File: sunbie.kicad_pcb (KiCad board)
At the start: 2 copper layers, 98 x 98 mm, 22 parts, among them J1 Display, Q1 BC547, SW1 SW_Push_45deg, SW2 SW_Push_45deg, SW3 SW_Push_45deg, SW4 SW_Push_45deg, SW5 SW_Push_45deg, U1 XIAO-ESP32-C3-SMD, U2 LSM6DS3, U3 BME280, U4 TSL25911FN

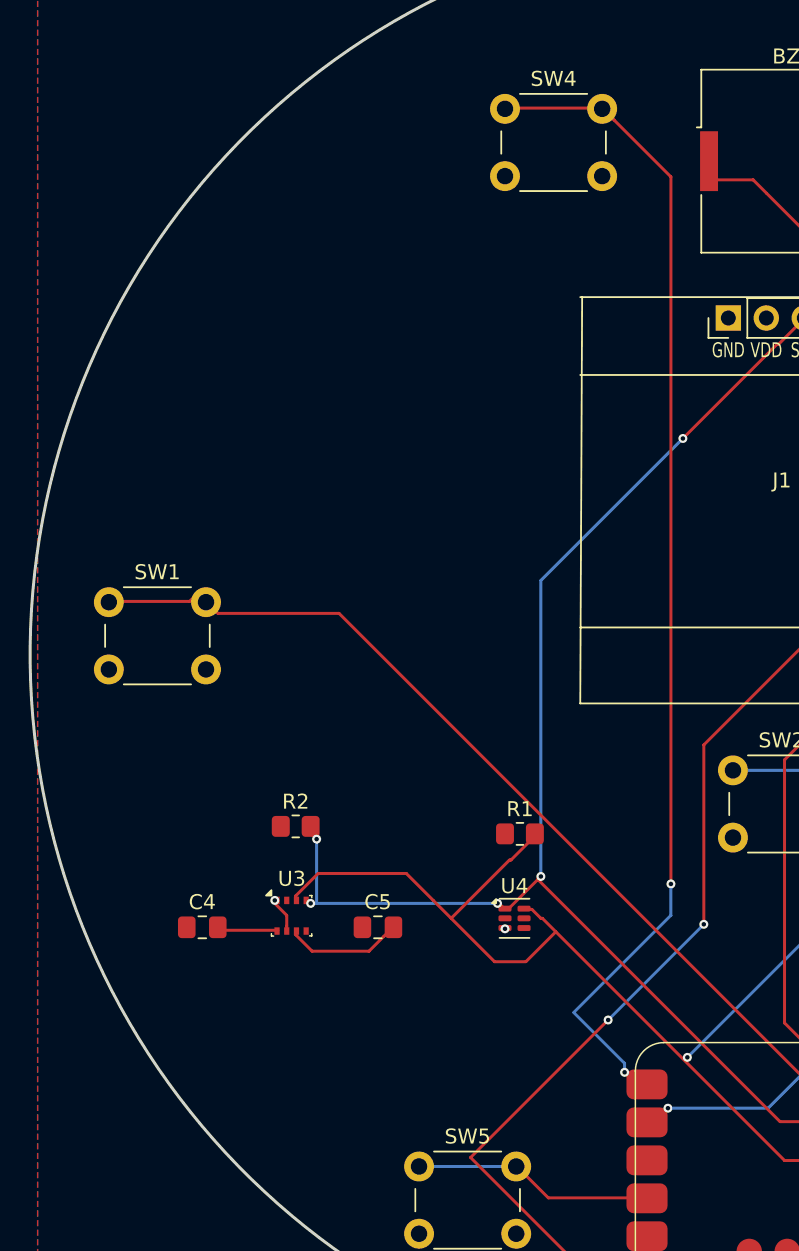
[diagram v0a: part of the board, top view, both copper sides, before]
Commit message: added 2 ws2812 leds
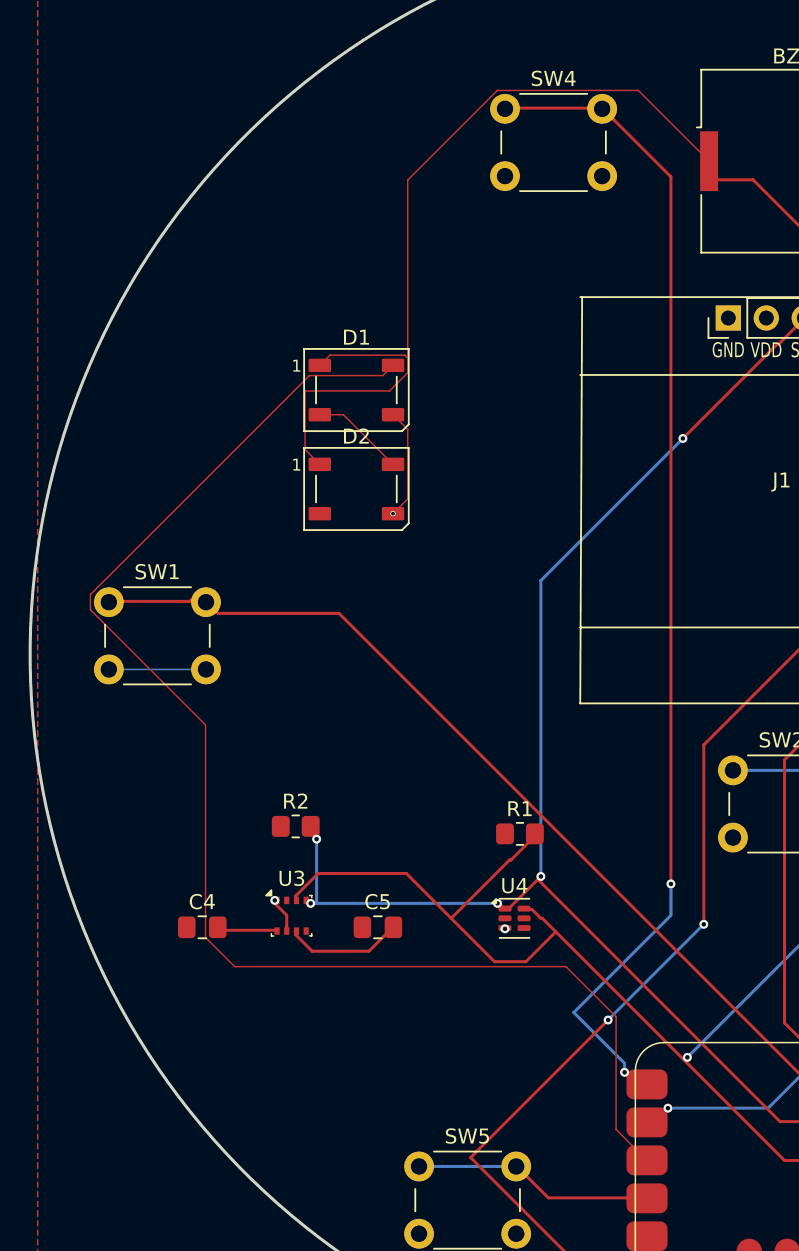
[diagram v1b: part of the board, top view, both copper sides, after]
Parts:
- added D1: WS2812B, LED_SMD:LED_WS2812B_PLCC4_5.0x5.0mm_P3.2mm, F.Cu at (77.1, 84.1)
- added D2: WS2812B, LED_SMD:LED_WS2812B_PLCC4_5.0x5.0mm_P3.2mm, F.Cu at (77.1, 90.7)
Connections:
- U1 pad 10: unconnected-(U1-D9/BOOT-Pad10) -> /LED_DATA
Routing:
- net /LED_DATA: track 0.00 -> 92.8 mm
- net +5V: track 114.7 -> 171.1 mm
- net GND: track 28.4 -> 42.4 mm, vias 10 -> 11
- net Net-(D1-DOUT): track 0.00 -> 6.28 mm
